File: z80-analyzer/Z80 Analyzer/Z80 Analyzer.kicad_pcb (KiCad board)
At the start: 2 copper layers, 65 x 65 mm, 48 parts, among them J1 Conn_01x40_Pin, M1 TestPoint, U1 Z80CPU

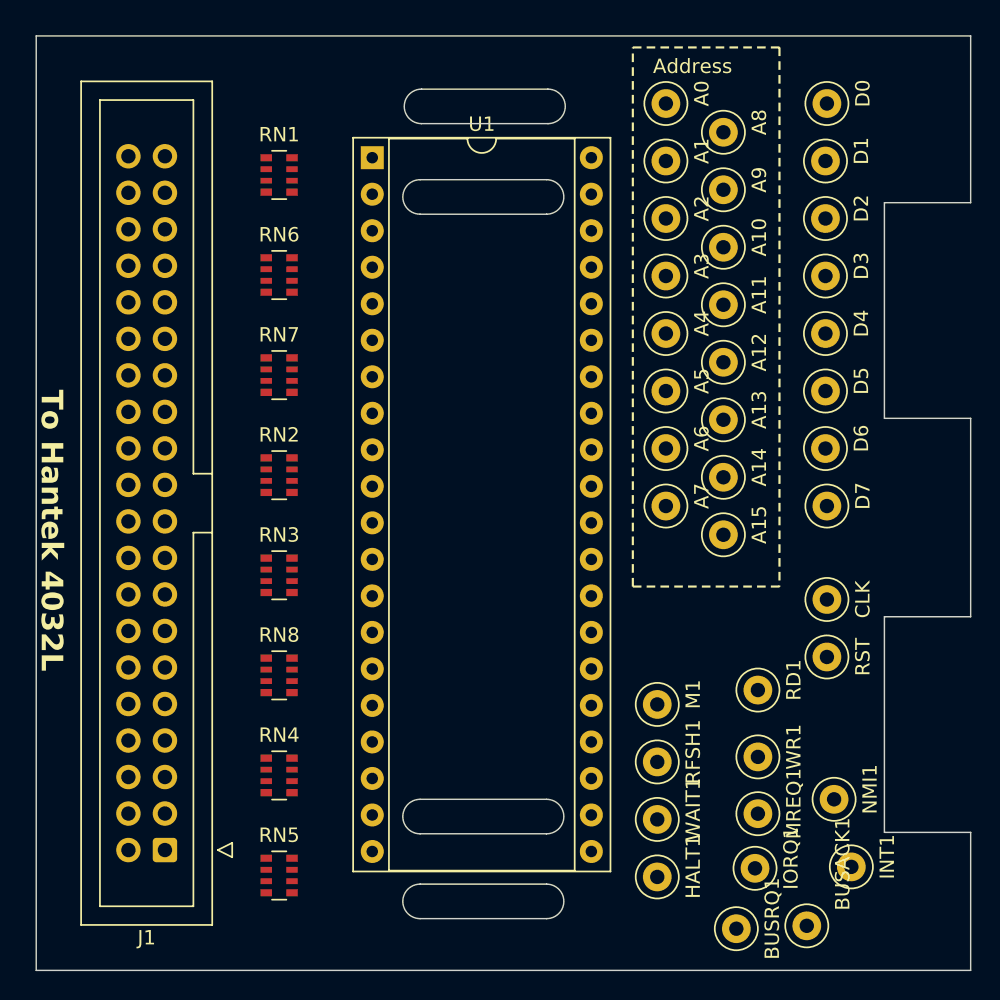
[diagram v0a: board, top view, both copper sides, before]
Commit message: [Z80] Layout update
Mostly done, missing:
* Size
* Aligned slots for socket stack securing
* Grounding lead pads
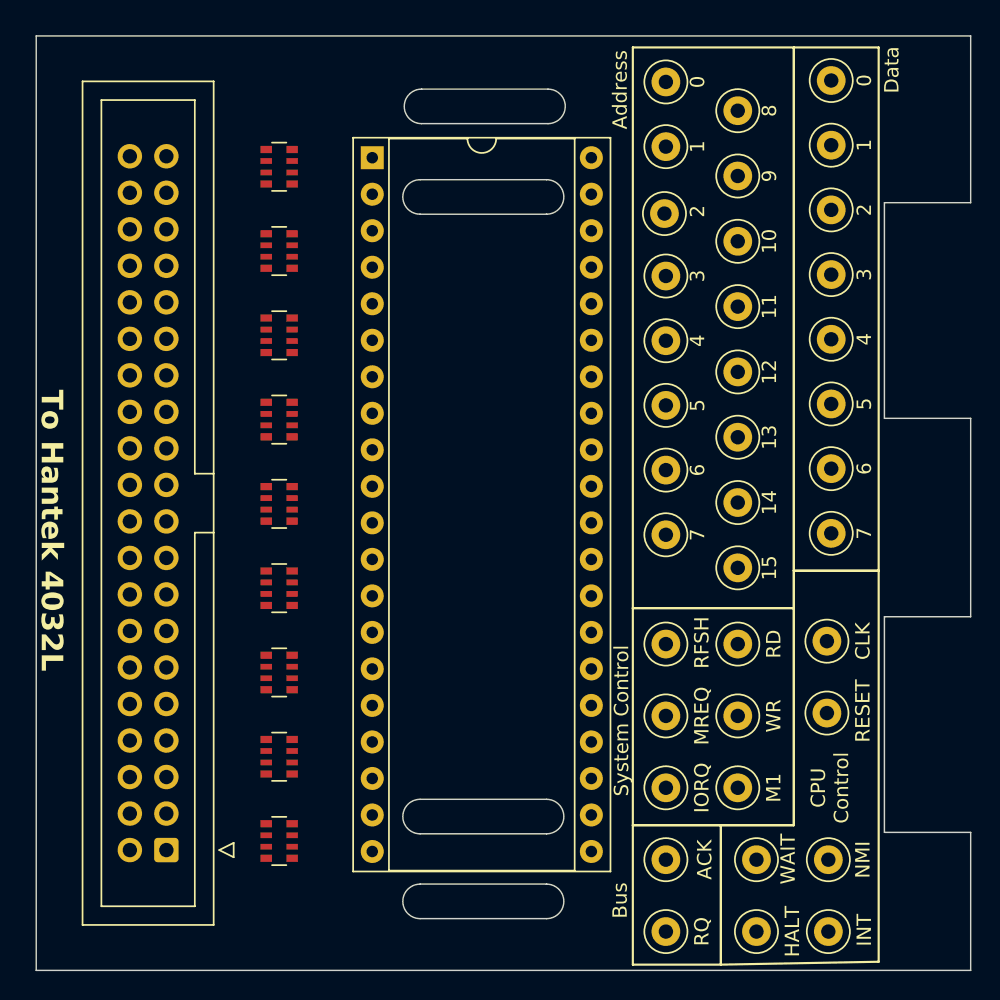
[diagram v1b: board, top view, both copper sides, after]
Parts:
- added RN9: R_Pack04_SIP_Split, Resistor_SMD:R_Array_Convex_4x0603, F.Cu at (138.1, 114.4)
- RN2, RN6: value R_Pack04_SIP_Split -> R_Pack04_Split
- moved RN4 42.3 mm to (138.1, 67.5), turned to 180 degrees
- moved RN8 29.5 mm to (138.1, 73.4), turned to 180 degrees
- moved RN1 22.9 mm to (138.1, 91.0), turned to 180 degrees
- moved RN6 21.8 mm to (138.1, 96.8), turned to 180 degrees
- moved RN3 16.7 mm to (138.1, 79.2), turned to 180 degrees
- moved RN2 13.7 mm to (138.1, 102.7), turned to 180 degrees
- moved BUSACK1 10.8 mm to (165.0, 115.7)
- moved MREQ1 9.34 mm to (165.0, 105.7)
- moved IORQ1 8.35 mm to (165.0, 110.7)
- moved RN5 8.26 mm to (138.1, 108.5), turned to 180 degrees
- moved RFSH1 8.22 mm to (165.0, 100.7)
- moved M1 8.06 mm to (170.0, 110.7)
- moved HALT1 7.88 mm to (171.3, 120.7)
- moved WAIT1 7.45 mm to (171.3, 115.7)
- moved BUSRQ1 4.90 mm to (165.0, 120.7)
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- renumbered CLK to CLK1, RST to RESET1
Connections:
- net /A0 renamed /S_A0
- net /A12 renamed /S_A12
- net /A4 renamed /S_A4
- net /A8 renamed /S_A8
- net /BUSACK renamed /S_BUSACK
- net /BUSRQ renamed /S_BUSRQ
- net /D0 renamed /S_D0
- net /D4 renamed /S_D4
- net /HALT renamed /S_HALT
- net /RFSH renamed /S_RFSH
- net /WAIT renamed /S_WAIT
- net /WR renamed /S_WR
- A1 pad 1: /A1 -> /S_A1
- A10 pad 1: /A10 -> /S_A10
- A11 pad 1: /A11 -> /S_A11
- A13 pad 1: /A13 -> /S_A13
- A14 pad 1: /A14 -> /S_A14
- A15 pad 1: /A15 -> /S_A15
- A2 pad 1: /A2 -> /S_A2
- A3 pad 1: /A3 -> /S_A3
- A5 pad 1: /A5 -> /S_A5
- A6 pad 1: /A6 -> /S_A6
- A7 pad 1: /A7 -> /S_A7
- A9 pad 1: /A9 -> /S_A9
- CLK1 pad 1: /CLK -> /S_CLK
- D1 pad 1: /D1 -> /S_D1
- D2 pad 1: /D2 -> /S_D2
- D3 pad 1: /D3 -> /S_D3
- D5 pad 1: /D5 -> /S_D5
- D6 pad 1: /D6 -> /S_D6
- D7 pad 1: /D7 -> /S_D7
- INT1 pad 1: /INT -> /S_INT
- IORQ1 pad 1: /IORQ -> /S_IORQ
- J1 pad 24: unconnected-(J1-Pin_24-Pad24) -> Net-(J1-Pin_24)
- J1 pad 26: unconnected-(J1-Pin_26-Pad26) -> Net-(J1-Pin_26)
- J1 pad 28: unconnected-(J1-Pin_28-Pad28) -> Net-(J1-Pin_28)
- J1 pad 3: unconnected-(J1-Pin_3-Pad3) -> Net-(J1-Pin_3)
- J1 pad 30: unconnected-(J1-Pin_30-Pad30) -> Net-(J1-Pin_30)
- J1 pad 32: unconnected-(J1-Pin_32-Pad32) -> Net-(J1-Pin_32)
- J1 pad 34: unconnected-(J1-Pin_34-Pad34) -> Net-(J1-Pin_34)
- J1 pad 36: unconnected-(J1-Pin_36-Pad36) -> Net-(J1-Pin_36)
- J1 pad 38: unconnected-(J1-Pin_38-Pad38) -> Net-(J1-Pin_38)
- J1 pad 4: unconnected-(J1-Pin_4-Pad4) -> Net-(J1-Pin_4)
- M1 pad 1: /M1 -> /S_M1
- MREQ1 pad 1: /MREQ -> /S_MREQ
- NMI1 pad 1: /NMI -> /S_NMI
- RD1 pad 1: /RD -> /S_RD
- RESET1 pad 1: /RESET -> /S_RESET
- RN1 pad 2: Net-(J1-Pin_15) -> /S_A5
- RN1 pad 3: /A5 -> /S_A6
- RN1 pad 4: Net-(J1-Pin_17) -> /S_A7
- RN1 pad 5: /A6 -> Net-(J1-Pin_21)
- RN1 pad 7: /A7 -> Net-(J1-Pin_17)
- RN1 pad 8: Net-(J1-Pin_21) -> Net-(J1-Pin_15)
- RN2 pad 2: Net-(J1-Pin_7) -> /S_A1
- RN2 pad 3: /A1 -> /S_A2
- RN2 pad 4: Net-(J1-Pin_9) -> /S_A3
- RN2 pad 5: /A2 -> Net-(J1-Pin_13)
- RN2 pad 7: /A3 -> Net-(J1-Pin_9)
- RN2 pad 8: Net-(J1-Pin_13) -> Net-(J1-Pin_7)
- RN3 pad 2: Net-(J1-Pin_23) -> /S_A9
- RN3 pad 3: /A9 -> /S_A10
- RN3 pad 4: Net-(J1-Pin_25) -> /S_A11
- RN3 pad 5: /A10 -> Net-(J1-Pin_29)
- RN3 pad 7: /A11 -> Net-(J1-Pin_25)
- RN3 pad 8: Net-(J1-Pin_29) -> Net-(J1-Pin_23)
- RN4 pad 2: Net-(J1-Pin_31) -> /S_A13
- RN4 pad 3: /A13 -> /S_A14
- RN4 pad 4: Net-(J1-Pin_33) -> /S_A15
- RN4 pad 5: /A14 -> Net-(J1-Pin_37)
- RN4 pad 7: /A15 -> Net-(J1-Pin_33)
- RN4 pad 8: Net-(J1-Pin_37) -> Net-(J1-Pin_31)
- RN5 pad 2: Net-(J1-Pin_8) -> /S_D1
- RN5 pad 3: /D1 -> /S_D2
- RN5 pad 4: Net-(J1-Pin_10) -> /S_D3
- RN5 pad 5: /D2 -> Net-(J1-Pin_14)
- RN5 pad 7: /D3 -> Net-(J1-Pin_10)
- RN5 pad 8: Net-(J1-Pin_14) -> Net-(J1-Pin_8)
- RN6 pad 2: Net-(J1-Pin_16) -> /S_D5
- RN6 pad 3: /D5 -> /S_D6
- RN6 pad 4: Net-(J1-Pin_18) -> /S_D7
- RN6 pad 5: /D6 -> Net-(J1-Pin_22)
- RN6 pad 7: /D7 -> Net-(J1-Pin_18)
- RN6 pad 8: Net-(J1-Pin_22) -> Net-(J1-Pin_16)
- RN7 pad 2: unconnected-(RN7A-R1.2-Pad2) -> /S_RD
- RN7 pad 3: /RD -> /S_IORQ
- RN7 pad 4: unconnected-(RN7B-R2.2-Pad4) -> /S_MREQ
- RN7 pad 5: /IORQ -> Net-(J1-Pin_30)
- RN7 pad 6: unconnected-(RN7C-R3.2-Pad6) -> Net-(J1-Pin_28)
- RN7 pad 7: /MREQ -> Net-(J1-Pin_26)
- RN7 pad 8: unconnected-(RN7D-R4.2-Pad8) -> Net-(J1-Pin_24)
- RN8 pad 1: /CLK -> /S_RESET
- RN8 pad 2: unconnected-(RN8A-R1.2-Pad2) -> /S_M1
- RN8 pad 3: /M1 -> /S_INT
- RN8 pad 4: unconnected-(RN8B-R2.2-Pad4) -> /S_NMI
- RN8 pad 5: /INT -> Net-(J1-Pin_38)
- RN8 pad 6: unconnected-(RN8C-R3.2-Pad6) -> Net-(J1-Pin_36)
- RN8 pad 7: /NMI -> Net-(J1-Pin_34)
- RN8 pad 8: unconnected-(RN8D-R4.2-Pad8) -> Net-(J1-Pin_32)
- U1 pad 1: /A11 -> /S_A11
- U1 pad 10: /D6 -> /S_D6
- U1 pad 12: /D2 -> /S_D2
- U1 pad 13: /D7 -> /S_D7
- U1 pad 15: /D1 -> /S_D1
- U1 pad 16: /INT -> /S_INT
- U1 pad 17: /NMI -> /S_NMI
- U1 pad 19: /MREQ -> /S_MREQ
- U1 pad 20: /IORQ -> /S_IORQ
- U1 pad 21: /RD -> /S_RD
- U1 pad 26: /RESET -> /S_RESET
- U1 pad 27: /M1 -> /S_M1
- U1 pad 3: /A13 -> /S_A13
- U1 pad 31: /A1 -> /S_A1
- U1 pad 32: /A2 -> /S_A2
- U1 pad 33: /A3 -> /S_A3
- U1 pad 35: /A5 -> /S_A5
- U1 pad 36: /A6 -> /S_A6
- U1 pad 37: /A7 -> /S_A7
- U1 pad 39: /A9 -> /S_A9
- U1 pad 4: /A14 -> /S_A14
- U1 pad 40: /A10 -> /S_A10
- U1 pad 5: /A15 -> /S_A15
- U1 pad 6: /CLK -> /S_CLK
- U1 pad 8: /D3 -> /S_D3
- U1 pad 9: /D5 -> /S_D5
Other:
- board text added: "0"
- board text added: "1"
- board text added: "10"
- board text added: "11"
- board text added: "12"
- board text added: "13"
- board text added: "14"
- board text added: "15"
- board text added: "2"
- board text added: "3"
- board text added: "4"
- board text added: "5"
- board text added: "6"
- board text added: "7"
- board text added: "8"
- board text added: "9"
- board text added: "ACK"
- board text added: "Bus"
- board text added: "CLK"
- board text added: "CPU Control"
- board text added: "Data"
- board text added: "HALT"
- board text added: "INT"
- board text added: "IORQ"
- board text added: "M1"
- board text added: "MREQ"
- board text added: "NMI"
- board text added: "RD"
- board text added: "RESET"
- board text added: "RFSH"
- board text added: "RQ"
- board text added: "System Control"
- board text added: "WAIT"
- board text added: "WR"
- board text removed: "TP min clearance: 4 or 5 mm, TBD"

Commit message: [Z80] Layout done
Needs ground vias, routing and some easter eggs
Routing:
- net Net-(J1-Pin_31): track 0.00 -> 11.1 mm
- net Net-(J1-Pin_33): track 0.00 -> 9.64 mm
- net Net-(J1-Pin_35): track 0.00 -> 8.92 mm
- net Net-(J1-Pin_37): track 0.00 -> 8.19 mm
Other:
- outline, holes or cut-outs redrawn
- board text added: ":)"
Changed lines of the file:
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@@
   (gr_rect (start 162.7 113.3) (end 168.8254 123)
     (stroke (width 0.15) (type solid)) (fill none) (layer "F.SilkS"))
-  (gr_rect (start 180.2 65.8) (end 186.1 70)
+  (gr_rect (start 180.2 62.9) (end 186.2 118.9)
+    (stroke (width 0.15) (type solid)) (fill solid) (layer "B.Mask"))
+  (gr_rect (start 180.2 62.9) (end 186.2 118.9)
     (stroke (width 0.15) (type solid)) (fill solid) (layer "F.Mask"))
-  (gr_line (start 147.9 68.4) (end 156.7 68.4)
-    (stroke (width 0.1) (type default)) (layer "Edge.Cuts"))
-  (gr_line (start 147.9 70.8) (end 156.7 70.8)
+  (gr_line (start 147.7 69) (end 156.5 69)
+    (stroke (width 0.1) (type default)) (layer "Edge.Cuts"))
+  (gr_line (start 147.7 71.4) (end 156.5 71.4)
     (stroke (width 0.1) (type default)) (layer "Edge.Cuts"))
   (gr_line (start 180.2 85) (end 186.2 85)
     (stroke (width 0.1) (type default)) (layer "Edge.Cuts"))
-  (gr_arc (start 148 64.5) (mid 146.8 63.3) (end 148 62.1)
-    (stroke (width 0.1) (type default)) (layer "Edge.Cuts"))
-  (gr_arc (start 147.9 119.8) (mid 146.7 118.6) (end 147.9 117.4)
-    (stroke (width 0.1) (type default)) (layer "Edge.Cuts"))
-  (gr_line (start 186.2 123.4) (end 121.2 123.4)
-    (stroke (width 0.1) (type default)) (layer "Edge.Cuts"))
-  (gr_line (start 147.9 119.8) (end 156.7 119.8)
-    (stroke (width 0.1) (type default)) (layer "Edge.Cuts"))
-  (gr_line (start 147.9 111.5) (end 156.7 111.5)
+  (gr_arc (start 147.7 65) (mid 146.5 63.8) (end 147.7 62.6)
+    (stroke (width 0.1) (type default)) (layer "Edge.Cuts"))
+  (gr_arc (start 147.7 119.4) (mid 146.5 118.2) (end 147.7 117)
+    (stroke (width 0.1) (type default)) (layer "Edge.Cuts"))
+  (gr_line (start 184.2 123.4) (end 123.214214 123.385786)
+    (stroke (width 0.1) (type default)) (layer "Edge.Cuts"))
+  (gr_arc (start 184.2 58.4) (mid 185.614214 58.985786) (end 186.2 60.4)
+    (stroke (width 0.1) (type default)) (layer "Edge.Cuts"))
+  (gr_line (start 147.7 119.4) (end 156.5 119.4)
+    (stroke (width 0.1) (type default)) (layer "Edge.Cuts"))
+  (gr_line (start 147.7 110.6) (end 156.5 110.6)
     (stroke (width 0.1) (type default)) (layer "Edge.Cuts"))
   (gr_line (start 180.2 98.8) (end 180.2 113.8)
@@
   (gr_line (start 180.2 70) (end 180.2 85)
     (stroke (width 0.1) (type default)) (layer "Edge.Cuts"))
-  (gr_arc (start 156.7 117.4) (mid 157.9 118.6) (end 156.7 119.8)
-    (stroke (width 0.1) (type default)) (layer "Edge.Cuts"))
-  (gr_arc (start 156.7 111.5) (mid 157.9 112.7) (end 156.7 113.9)
-    (stroke (width 0.1) (type default)) (layer "Edge.Cuts"))
-  (gr_arc (start 147.9 70.8) (mid 146.7 69.6) (end 147.9 68.4)
+  (gr_arc (start 156.5 117) (mid 157.7 118.2) (end 156.5 119.4)
+    (stroke (width 0.1) (type default)) (layer "Edge.Cuts"))
+  (gr_arc (start 156.5 110.6) (mid 157.7 111.8) (end 156.5 113)
+    (stroke (width 0.1) (type default)) (layer "Edge.Cuts"))
+  (gr_arc (start 147.7 71.4) (mid 146.5 70.2) (end 147.7 69)
     (stroke (width 0.1) (type default)) (layer "Edge.Cuts"))
   (gr_line (start 186.2 85) (end 186.2 98.8)
     (stroke (width 0.1) (type default)) (layer "Edge.Cuts"))
-  (gr_line (start 186.2 58.4) (end 186.2 70)
-    (stroke (width 0.1) (type default)) (layer "Edge.Cuts"))
-  (gr_arc (start 156.7 68.4) (mid 157.9 69.6) (end 156.7 70.8)
+  (gr_line (start 186.2 60.4) (end 186.2 70)
+    (stroke (width 0.1) (type default)) (layer "Edge.Cuts"))
+  (gr_arc (start 156.5 69) (mid 157.7 70.2) (end 156.5 71.4)
     (stroke (width 0.1) (type default)) (layer "Edge.Cuts"))
   (gr_line (start 180.2 113.8) (end 186.2 113.8)
     (stroke (width 0.1) (type default)) (layer "Edge.Cuts"))
+  (gr_arc (start 123.214214 123.385786) (mid 121.8 122.8) (end 121.214214 121.385786)
+    (stroke (width 0.1) (type default)) (layer "Edge.Cuts"))
   (gr_line (start 186.2 98.8) (end 180.2 98.8)
     (stroke (width 0.1) (type default)) (layer "Edge.Cuts"))
-  (gr_line (start 121.2 123.4) (end 121.2 58.4)
-    (stroke (width 0.1) (type default)) (layer "Edge.Cuts"))
-  (gr_line (start 148 64.5) (end 156.8 64.5)
-    (stroke (width 0.1) (type default)) (layer "Edge.Cuts"))
-  (gr_line (start 147.9 113.9) (end 156.7 113.9)
-    (stroke (width 0.1) (type default)) (layer "Edge.Cuts"))
-  (gr_line (start 121.2 58.4) (end 186.2 58.4)
-    (stroke (width 0.1) (type default)) (layer "Edge.Cuts"))
-  (gr_line (start 148 62.1) (end 156.8 62.1)
-    (stroke (width 0.1) (type default)) (layer "Edge.Cuts"))
-  (gr_line (start 147.9 117.4) (end 156.7 117.4)
-    (stroke (width 0.1) (type default)) (layer "Edge.Cuts"))
-  (gr_arc (start 147.9 113.9) (mid 146.7 112.7) (end 147.9 111.5)
-    (stroke (width 0.1) (type default)) (layer "Edge.Cuts"))
-  (gr_arc (start 156.8 62.1) (mid 158 63.3) (end 156.8 64.5)
-    (stroke (width 0.1) (type default)) (layer "Edge.Cuts"))
-  (gr_line (start 186.2 113.8) (end 186.2 123.4)
+  (gr_line (start 121.214214 121.385786) (end 121.204841 60.436842)
+    (stroke (width 0.1) (type default)) (layer "Edge.Cuts"))
+  (gr_line (start 147.7 65) (end 156.5 65)
+    (stroke (width 0.1) (type default)) (layer "Edge.Cuts"))
+  (gr_line (start 147.7 113) (end 156.5 113)
+    (stroke (width 0.1) (type default)) (layer "Edge.Cuts"))
+  (gr_line (start 123.236841 58.404841) (end 184.2 58.4)
+    (stroke (width 0.1) (type default)) (layer "Edge.Cuts"))
+  (gr_line (start 147.7 62.6) (end 156.5 62.6)
+    (stroke (width 0.1) (type default)) (layer "Edge.Cuts"))
+  (gr_line (start 147.7 117) (end 156.5 117)
+    (stroke (width 0.1) (type default)) (layer "Edge.Cuts"))
+  (gr_arc (start 147.7 113) (mid 146.5 111.8) (end 147.7 110.6)
+    (stroke (width 0.1) (type default)) (layer "Edge.Cuts"))
+  (gr_arc (start 121.204841 60.436842) (mid 121.8 59) (end 123.236841 58.404841)
+    (stroke (width 0.1) (type default)) (layer "Edge.Cuts"))
+  (gr_arc (start 156.5 62.6) (mid 157.7 63.8) (end 156.5 65)
+    (stroke (width 0.1) (type default)) (layer "Edge.Cuts"))
+  (gr_arc (start 186.2 121.4) (mid 185.614214 122.814214) (end 184.2 123.4)
+    (stroke (width 0.1) (type default)) (layer "Edge.Cuts"))
+  (gr_line (start 186.2 113.8) (end 186.2 121.4)
     (stroke (width 0.1) (type default)) (layer "Edge.Cuts"))
   (gr_text "Bus" (at 162.4 119.8 90) (layer "F.SilkS")
@@
   (gr_text "0" (at 167.2 61.6 90) (layer "F.SilkS")
     (effects (font (size 1 1) (thickness 0.15)))
+  )
+  (gr_text ":)" (at 182.6 121.6) (layer "F.SilkS")
+    (effects (font (size 1 1) (thickness 0.15)) (justify left bottom))
   )
   (gr_text "9" (at 172.2 68.142857 90) (layer "F.SilkS")
@@
     (effects (font (size 1 1) (thickness 0.15)))
   )
-  (gr_text "To Hantek 4032L" (at 121.4 83 270) (layer "F.SilkS")
+  (gr_text "To Hantek 4032L" (at 121.8 83 270) (layer "F.SilkS")
     (effects (font (size 1.5 1.5) (thickness 0.3) bold) (justify left bottom))
   )
@@
     (effects (font (size 1 1) (thickness 0.15)))
   )
+  (segment (start 137.2 68.7) (end 137.2 69.9825) (width 0.25) (layer "F.Cu") (net 21))
+  (segment (start 137.2 69.9825) (end 130.2525 76.93) (width 0.25) (layer "F.Cu") (net 21))
+  (segment (start 136.7425 67.9) (end 130.2525 74.39) (width 0.25) (layer "F.Cu") (net 22))
+  (segment (start 137.2 67.9) (end 136.7425 67.9) (width 0.25) (layer "F.Cu") (net 22))
+  (segment (start 137.2 67.1) (end 135.0025 67.1) (width 0.25) (layer "F.Cu") (net 23))
+  (segment (start 135.0025 67.1) (end 130.2525 71.85) (width 0.25) (layer "F.Cu") (net 23))
+  (segment (start 137.2 66.3) (end 133.2625 66.3) (width 0.25) (layer "F.Cu") (net 24))
+  (segment (start 133.2625 66.3) (end 130.2525 69.31) (width 0.25) (layer "F.Cu") (net 24))
+  (group "" (id 031dcdb3-54cd-4119-bc2c-c3576091616a)
+    (members
+      0e25c8cb-abe6-4394-862f-38e3b2c11115
+      64540630-f56e-411b-8925-e2e3d528d636
+    )
+  )
   (group "" (id 135c612a-aa26-47a2-8a40-20a4ea95025d)
